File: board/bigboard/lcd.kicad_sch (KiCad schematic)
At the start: 5 parts, among them J8 Conn_2Rows-21Pins_MountingPin, U5 SN74LVCH8T245PWR, U6 SN74LVCH8T245PWR

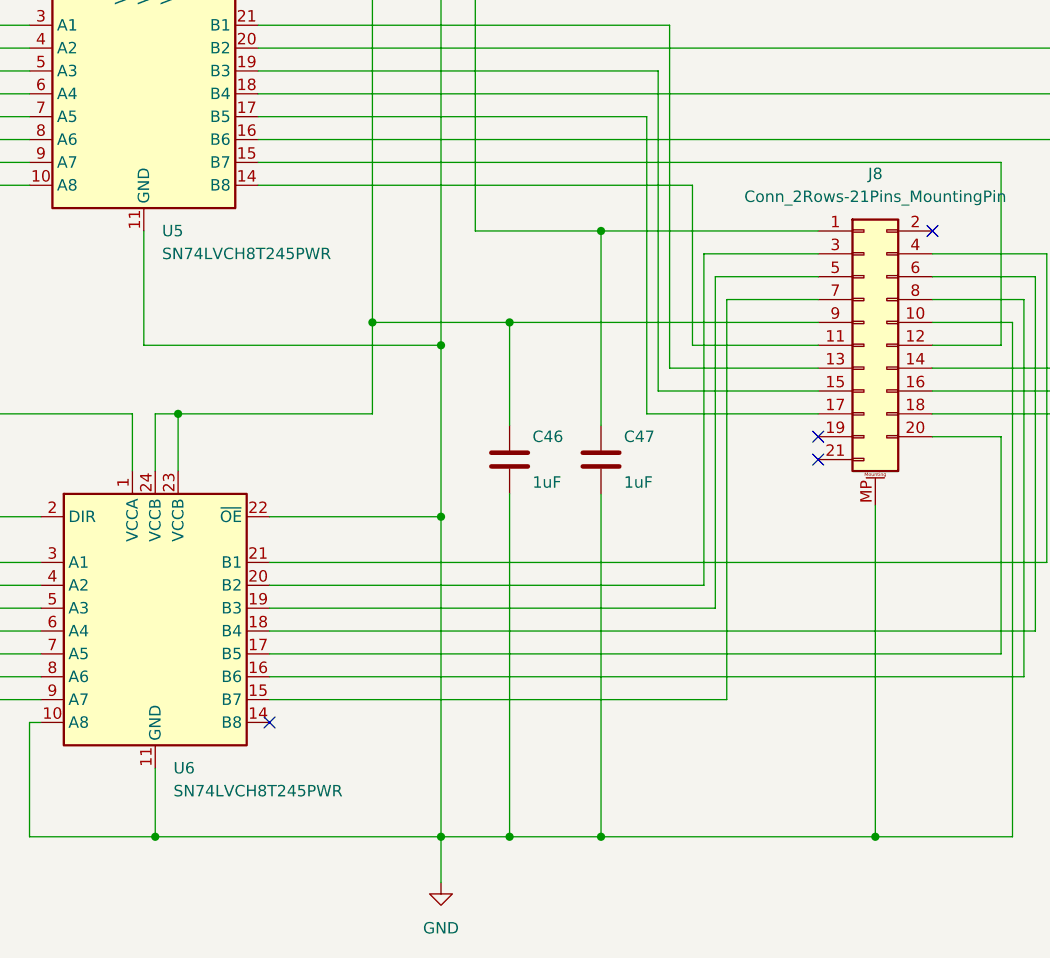
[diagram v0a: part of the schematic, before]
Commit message: Manufactured version of bigboard
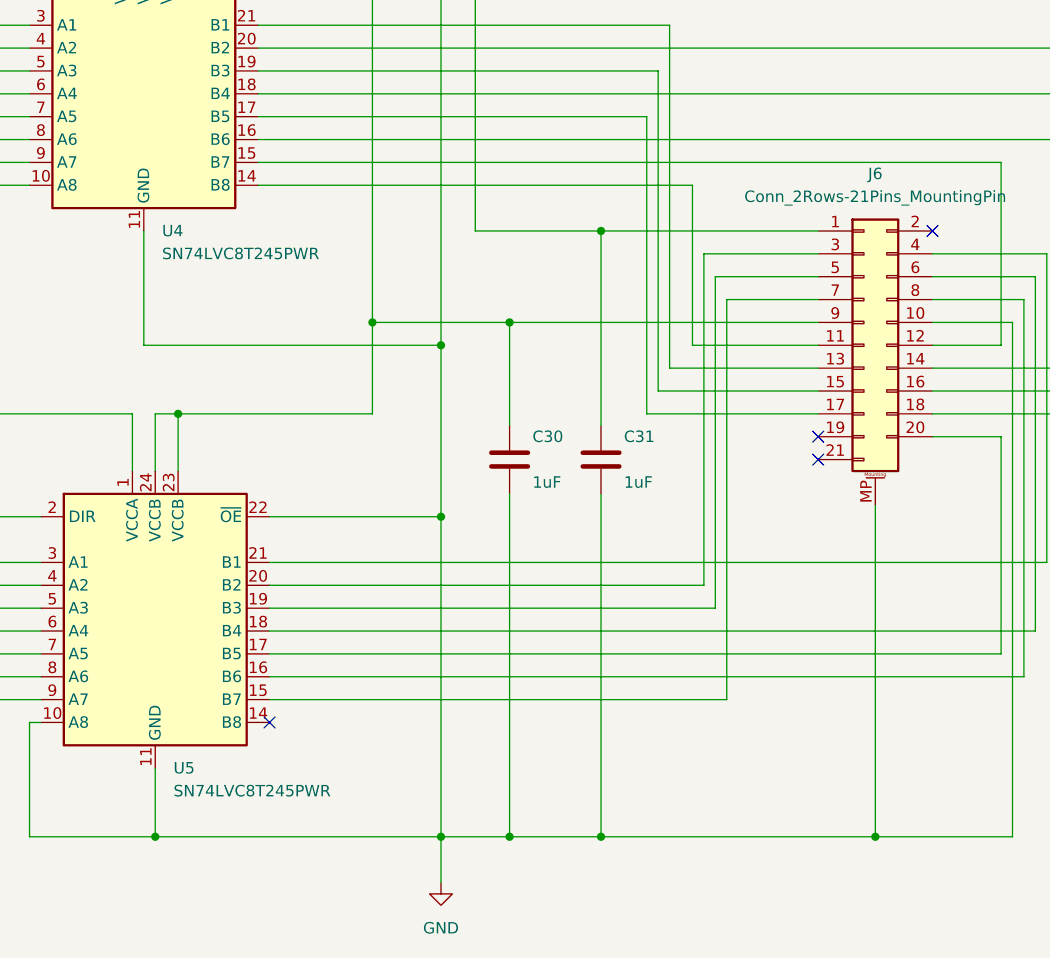
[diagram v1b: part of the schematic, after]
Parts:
- C30: renamed from C46; MPN (none) -> CC0201MRX5R6BB105
- C31: renamed from C47; MPN (none) -> CC0201MRX5R6BB105
- U4: renamed from U5; value SN74LVCH8T245PWR -> SN74LVC8T245PWR; MPN SN74LVCH8T245PWR -> SN74LVC8T245PWR
- U5: renamed from U6; value SN74LVCH8T245PWR -> SN74LVC8T245PWR; MPN SN74LVCH8T245PWR -> SN74LVC8T245PWR
- renumbered J8 to J6
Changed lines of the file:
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@@
   (symbol (lib_id "Logic_LevelTranslator:SN74AVC8T245PW") (at 158.75 55.88 0) (unit 1)
     (in_bom yes) (on_board yes) (fields_autoplaced)
-    (property "Reference" "U5" (id 0) (at 160.7694 73.66 0)
-      (effects (font (size 1.27 1.27)) (justify left))
-    )
-    (property "Value" "SN74LVCH8T245PWR" (id 1) (at 160.7694 76.2 0)
+    (property "Reference" "U4" (id 0) (at 160.7694 73.66 0)
+      (effects (font (size 1.27 1.27)) (justify left))
+    )
+    (property "Value" "SN74LVC8T245PWR" (id 1) (at 160.7694 76.2 0)
       (effects (font (size 1.27 1.27)) (justify left))
     )
@@
       (effects (font (size 1.27 1.27)) hide)
     )
-    (property "MPN" "SN74LVCH8T245PWR" (id 4) (at 158.75 55.88 0)
+    (property "MPN" "SN74LVC8T245PWR" (id 4) (at 158.75 55.88 0)
       (effects (font (size 1.27 1.27)) hide)
     )
@@
   (symbol (lib_id "power:+1V8") (at 134.62 29.21 0) (unit 1)
     (in_bom yes) (on_board yes) (fields_autoplaced)
-    (property "Reference" "#PWR028" (id 0) (at 134.62 33.02 0)
+    (property "Reference" "#PWR024" (id 0) (at 134.62 33.02 0)
       (effects (font (size 1.27 1.27)) hide)
     )
@@
   (symbol (lib_id "power:+5V") (at 195.58 35.56 0) (unit 1)
     (in_bom yes) (on_board yes)
-    (property "Reference" "#PWR031" (id 0) (at 195.58 39.37 0)
+    (property "Reference" "#PWR027" (id 0) (at 195.58 39.37 0)
       (effects (font (size 1.27 1.27)) hide)
     )
@@
   (symbol (lib_id "Connector_Generic_MountingPin:Conn_2Rows-21Pins_MountingPin") (at 238.76 86.36 0) (unit 1)
     (in_bom yes) (on_board yes) (fields_autoplaced)
-    (property "Reference" "J8" (id 0) (at 240.03 67.31 0))
+    (property "Reference" "J6" (id 0) (at 240.03 67.31 0))
     (property "Value" "Conn_2Rows-21Pins_MountingPin" (id 1) (at 240.03 69.85 0))
     (property "Footprint" "displaymolex:5035662102" (id 2) (at 238.76 86.36 0)
@@
   (symbol (lib_id "Logic_LevelTranslator:SN74AVC8T245PW") (at 160.02 115.57 0) (unit 1)
     (in_bom yes) (on_board yes) (fields_autoplaced)
-    (property "Reference" "U6" (id 0) (at 162.0394 133.35 0)
-      (effects (font (size 1.27 1.27)) (justify left))
-    )
-    (property "Value" "SN74LVCH8T245PWR" (id 1) (at 162.0394 135.89 0)
+    (property "Reference" "U5" (id 0) (at 162.0394 133.35 0)
+      (effects (font (size 1.27 1.27)) (justify left))
+    )
+    (property "Value" "SN74LVC8T245PWR" (id 1) (at 162.0394 135.89 0)
       (effects (font (size 1.27 1.27)) (justify left))
     )
@@
       (effects (font (size 1.27 1.27)) hide)
     )
-    (property "MPN" "SN74LVCH8T245PWR" (id 4) (at 160.02 115.57 0)
+    (property "MPN" "SN74LVC8T245PWR" (id 4) (at 160.02 115.57 0)
       (effects (font (size 1.27 1.27)) hide)
     )
@@
   (symbol (lib_id "Device:C") (at 209.55 99.06 0) (unit 1)
     (in_bom yes) (on_board yes)
-    (property "Reference" "C47" (id 0) (at 212.09 96.52 0)
+    (property "Reference" "C31" (id 0) (at 212.09 96.52 0)
       (effects (font (size 1.27 1.27)) (justify left))
     )
@@
       (effects (font (size 1.27 1.27)) hide)
     )
-    (property "Description" "CAP CERM 1uF +/10% 25V X5R 0201" (id 4) (at 209.55 99.06 0)
+    (property "Description" "CAP CERM 1uF +/20% 10V X5R 0201" (id 4) (at 209.55 99.06 0)
+      (effects (font (size 1.27 1.27)) hide)
+    )
+    (property "MPN" "CC0201MRX5R6BB105" (id 5) (at 209.55 99.06 0)
       (effects (font (size 1.27 1.27)) hide)
     )
@@
   (symbol (lib_id "power:GND") (at 191.77 146.05 0) (unit 1)
     (in_bom yes) (on_board yes) (fields_autoplaced)
-    (property "Reference" "#PWR030" (id 0) (at 191.77 152.4 0)
+    (property "Reference" "#PWR026" (id 0) (at 191.77 152.4 0)
       (effects (font (size 1.27 1.27)) hide)
     )
@@
   (symbol (lib_id "3v2:+3V2") (at 184.15 29.21 0) (unit 1)
     (in_bom yes) (on_board yes) (fields_autoplaced)
-    (property "Reference" "#PWR029" (id 0) (at 184.15 33.02 0)
+    (property "Reference" "#PWR025" (id 0) (at 184.15 33.02 0)
       (effects (font (size 1.27 1.27)) hide)
     )
@@
   (symbol (lib_id "Device:C") (at 199.39 99.06 0) (unit 1)
     (in_bom yes) (on_board yes)
-    (property "Reference" "C46" (id 0) (at 201.93 96.52 0)
+    (property "Reference" "C30" (id 0) (at 201.93 96.52 0)
       (effects (font (size 1.27 1.27)) (justify left))
     )
@@
       (effects (font (size 1.27 1.27)) hide)
     )
-    (property "Description" "CAP CERM 1uF +/10% 25V X5R 0201" (id 4) (at 199.39 99.06 0)
-      (effects (font (size 1.27 1.27)) hide)
-    )
+    (property "Description" "CAP CERM 1uF +/20% 10V X5R 0201" (id 4) (at 199.39 99.06 0)
+      (effects (font (size 1.27 1.27)) hide)
+    )
+    (property "MPN" "CC0201MRX5R6BB105" (id 5) (at 199.39 99.06 0)
+      (effects (font (size 1.27 1.27)) hide)
+    )
